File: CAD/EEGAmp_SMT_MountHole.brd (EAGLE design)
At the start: 23.2 x 11.3 mm, 16 parts, among them U1 TL084QD

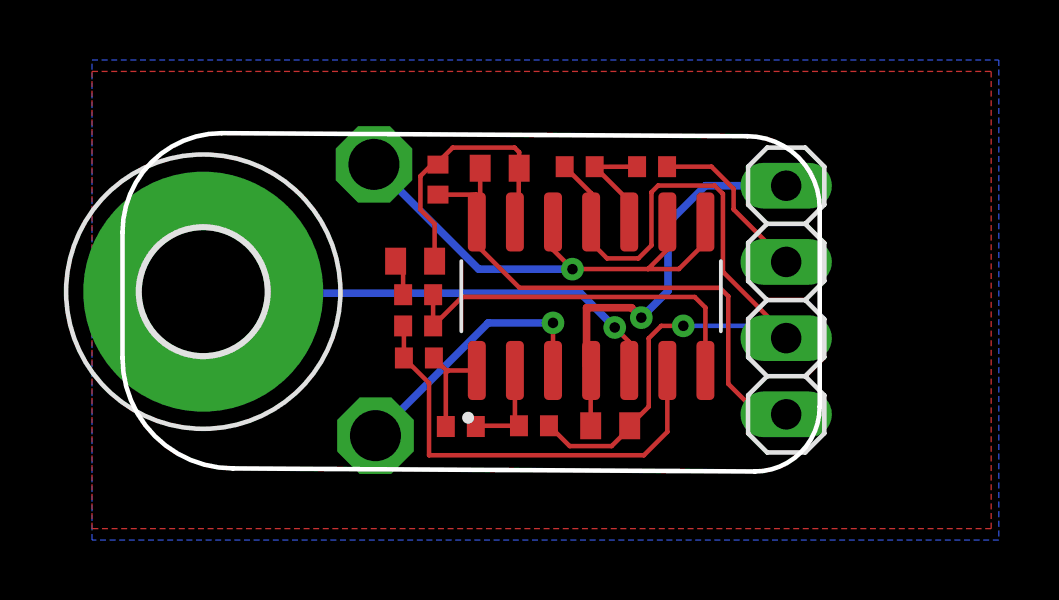
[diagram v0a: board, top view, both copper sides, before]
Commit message: added a filter cap on inputs
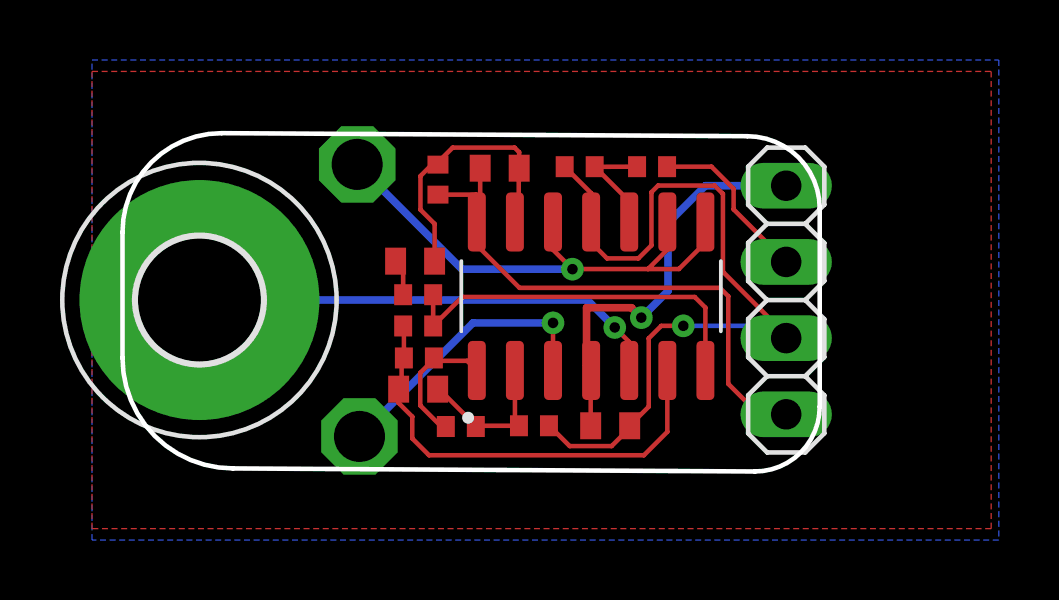
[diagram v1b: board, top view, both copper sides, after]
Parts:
- added C4: 2.2nF, rcl:C0402
- moved REFOUT 0.56 mm to (18.9, 29.8)
- moved AIN- 0.53 mm to (18.9, 20.7)
- moved H1 0.31 mm to (13.6, 25.3)
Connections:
- net 1IN-: now also C4.2
- net 2IN-: now also C4.1
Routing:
- net 1IN-: track 3.36 -> 5.14 mm
- net 1OUT: track 3.49 -> 4.52 mm
- net REFOUT: track 17.2 -> 17.8 mm
- net AIN-: track 9.06 -> 9.61 mm
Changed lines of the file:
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@@
 <plain>
 <text x="19.4564" y="24.638" size="1.778" layer="26" rot="MR0">+</text>
-<text x="16.8832" y="19.993715625" size="1.778" layer="26" rot="MR90">--</text>
+<text x="16.4514" y="19.993715625" size="1.778" layer="26" rot="MR90">--</text>
 <text x="30.018703125" y="29.145721875" size="1.016" layer="26" rot="MR90">V</text>
 <text x="29.983928125" y="24.661759375" size="1.016" layer="26" rot="MR90">VREF</text>
@@
 <attribute name="VALUE" x="29.9974" y="30.353" size="1.27" layer="27" rot="R270"/>
 </element>
-<element name="AIN-" library="testpad" library_urn="urn:adsk.eagle:library:385" package="P1-17" package3d_urn="urn:adsk.eagle:package:27949/1" value="PTR1PAD1-17" x="19.4818" y="20.7518" smashed="yes" rot="R90">
-<attribute name="POPULARITY" value="0" x="19.4818" y="20.7518" size="1.778" layer="27" rot="R90" display="off"/>
-<attribute name="TP_SIGNAL_NAME" value="" x="19.4818" y="20.7518" size="1.778" layer="27" rot="R90" display="off"/>
-</element>
-<element name="H1" library="holes" package="4,1-PAD" value="MOUNT-PAD-ROUND4.1" x="13.7414" y="25.5524" smashed="yes"/>
-<element name="REFOUT" library="testpad" library_urn="urn:adsk.eagle:library:385" package="P1-17" package3d_urn="urn:adsk.eagle:package:27949/1" value="PTR1PAD1-17" x="19.431" y="29.7942" smashed="yes">
-<attribute name="NAME" x="21.8948" y="27.4574" size="0.8128" layer="26" ratio="10" rot="MR0"/>
-<attribute name="POPULARITY" value="0" x="19.558" y="29.7942" size="1.778" layer="27" display="off"/>
-<attribute name="TP_SIGNAL_NAME" value="" x="18.161" y="26.6192" size="1" layer="37"/>
-<attribute name="VALUE" x="24.257" y="37.4142" size="0.0254" layer="27"/>
+<element name="AIN-" library="testpad" library_urn="urn:adsk.eagle:library:385" package="P1-17" package3d_urn="urn:adsk.eagle:package:27949/1" value="PTR1PAD1-17" x="18.9484" y="20.7264" smashed="yes" rot="R90">
+<attribute name="POPULARITY" value="0" x="18.9484" y="20.7264" size="1.778" layer="27" rot="R90" display="off"/>
+<attribute name="TP_SIGNAL_NAME" value="" x="18.9484" y="20.7264" size="1.778" layer="27" rot="R90" display="off"/>
+</element>
+<element name="H1" library="holes" package="4,1-PAD" value="MOUNT-PAD-ROUND4.1" x="13.6144" y="25.273" smashed="yes"/>
+<element name="REFOUT" library="testpad" library_urn="urn:adsk.eagle:library:385" package="P1-17" package3d_urn="urn:adsk.eagle:package:27949/1" value="PTR1PAD1-17" x="18.8722" y="29.7942" smashed="yes">
+<attribute name="NAME" x="21.336" y="27.4574" size="0.8128" layer="26" ratio="10" rot="MR0"/>
+<attribute name="POPULARITY" value="0" x="18.9992" y="29.7942" size="1.778" layer="27" display="off"/>
+<attribute name="TP_SIGNAL_NAME" value="" x="17.6022" y="26.6192" size="1" layer="37"/>
+<attribute name="VALUE" x="23.6982" y="37.4142" size="0.0254" layer="27"/>
+</element>
+<element name="C4" library="rcl" library_urn="urn:adsk.eagle:library:334" package="C0402" package3d_urn="urn:adsk.eagle:package:23626/2" value="2.2nF" x="20.9042" y="22.3012" smashed="yes">
+<attribute name="NAME" x="22.3012" y="21.6916" size="1.27" layer="26" rot="MR0"/>
+<attribute name="POPULARITY" value="16" x="20.9042" y="22.3012" size="1.778" layer="27" display="off"/>
+<attribute name="SPICEPREFIX" value="C" x="20.9042" y="22.3012" size="1.778" layer="27" display="off"/>
 </element>
 </elements>
@@
 <wire x1="25.4" y1="24.511" x2="25.4" y2="22.925" width="0.1524" layer="1"/>
 <contactref element="AIN-" pad="TP"/>
-<wire x1="19.4818" y1="20.7518" x2="23.241" y2="24.511" width="0.254" layer="16"/>
-<wire x1="23.241" y1="24.511" x2="25.4" y2="24.511" width="0.254" layer="16"/>
+<wire x1="18.9484" y1="20.7264" x2="22.733" y2="24.511" width="0.254" layer="16"/>
+<wire x1="22.733" y1="24.511" x2="25.4" y2="24.511" width="0.254" layer="16"/>
 </signal>
 <signal name="VREF">
@@
 <wire x1="27.4574" y1="24.3586" x2="27.94" y2="23.876" width="0.1524" layer="1"/>
 <wire x1="27.94" y1="23.876" x2="27.94" y2="22.925" width="0.1524" layer="1"/>
-<wire x1="27.4574" y1="24.3586" x2="26.3144" y2="25.5016" width="0.254" layer="16"/>
+<wire x1="27.4574" y1="24.3586" x2="26.543" y2="25.273" width="0.254" layer="16"/>
 <contactref element="H1" pad="B4,1"/>
-<wire x1="13.7922" y1="25.5016" x2="13.7414" y2="25.5524" width="0.254" layer="16"/>
-<wire x1="26.3144" y1="25.5016" x2="13.7922" y2="25.5016" width="0.254" layer="16"/>
+<wire x1="26.543" y1="25.273" x2="13.6144" y2="25.273" width="0.254" layer="16"/>
 </signal>
 <signal name="2IN-">
@@
 <wire x1="29.21" y1="22.925" x2="29.21" y2="20.8788" width="0.1524" layer="1"/>
 <wire x1="28.4298" y1="20.0986" x2="21.2678" y2="20.0986" width="0.1524" layer="1"/>
-<wire x1="21.2678" y1="22.5044" x2="20.4296" y2="23.3426" width="0.1524" layer="1"/>
-<wire x1="21.2678" y1="22.5044" x2="21.2678" y2="20.0986" width="0.1524" layer="1"/>
+<wire x1="21.2678" y1="20.0986" x2="20.709" y2="20.6574" width="0.1524" layer="1"/>
+<wire x1="20.709" y1="21.3868" x2="20.709" y2="20.6574" width="0.1524" layer="1"/>
 <wire x1="29.21" y1="20.8788" x2="28.4298" y2="20.0986" width="0.1524" layer="1"/>
 <wire x1="20.4042" y1="24.4094" x2="20.4296" y2="24.384" width="0.1524" layer="1"/>
 <wire x1="20.4296" y1="24.384" x2="20.4296" y2="23.3426" width="0.1524" layer="1"/>
+<contactref element="C4" pad="1"/>
+<wire x1="20.4296" y1="23.3426" x2="20.3534" y2="23.2664" width="0.1524" layer="1"/>
+<wire x1="20.3534" y1="23.2664" x2="20.3534" y2="22.4004" width="0.1524" layer="1"/>
+<wire x1="20.3534" y1="22.4004" x2="20.2542" y2="22.3012" width="0.1524" layer="1"/>
+<wire x1="20.709" y1="21.3868" x2="20.2542" y2="21.8416" width="0.1524" layer="1"/>
+<wire x1="20.2542" y1="22.3012" x2="20.2542" y2="21.8416" width="0.1524" layer="1"/>
 </signal>
 <signal name="3IN+">
@@
 <contactref element="R1" pad="1"/>
 <contactref element="R3" pad="2"/>
-<wire x1="21.898" y1="22.925" x2="22.86" y2="22.925" width="0.1524" layer="1"/>
-<wire x1="21.8266" y1="21.0566" x2="21.8266" y2="22.8536" width="0.1524" layer="1"/>
-<wire x1="21.8266" y1="22.8536" x2="21.8639" y2="22.8909" width="0.1524" layer="1"/>
-<wire x1="21.8639" y1="22.8909" x2="21.898" y2="22.925" width="0.1524" layer="1"/>
-<wire x1="21.4296" y1="23.3426" x2="21.8639" y2="22.9083" width="0.1524" layer="1"/>
-<wire x1="21.8639" y1="22.9083" x2="21.8639" y2="22.8909" width="0.1524" layer="1"/>
+<wire x1="22.86" y1="22.925" x2="22.5385" y2="23.2465" width="0.1524" layer="1"/>
+<wire x1="22.5385" y1="23.2465" x2="21.5257" y2="23.2465" width="0.1524" layer="1"/>
+<wire x1="21.4296" y1="23.3426" x2="21.5257" y2="23.2465" width="0.1524" layer="1"/>
+<wire x1="20.9756" y1="22.8458875" x2="20.9756" y2="21.7565125" width="0.1524" layer="1"/>
+<wire x1="20.9756" y1="21.7565125" x2="21.6683125" y2="21.0638" width="0.1524" layer="1"/>
+<wire x1="21.4296" y1="23.3426" x2="21.4296" y2="23.2998875" width="0.1524" layer="1"/>
+<wire x1="21.6683125" y1="21.0638" x2="21.8194" y2="21.0638" width="0.1524" layer="1"/>
+<wire x1="21.4296" y1="23.2998875" x2="20.9756" y2="22.8458875" width="0.1524" layer="1"/>
+<wire x1="21.8194" y1="21.0638" x2="21.8266" y2="21.0566" width="0.1524" layer="1"/>
 </signal>
 <signal name="VDD">
@@
 <wire x1="22.8266" y1="21.0566" x2="22.8266" y2="21.082" width="0.1524" layer="1"/>
 <wire x1="22.8266" y1="21.082" x2="24.265" y2="21.082" width="0.1524" layer="1"/>
+<contactref element="C4" pad="2"/>
+<wire x1="21.5542" y1="22.3012" x2="21.6074" y2="22.3012" width="0.1524" layer="1"/>
+<wire x1="21.6074" y1="22.3012" x2="22.8266" y2="21.082" width="0.1524" layer="1"/>
 </signal>
 <signal name="4IN-">
@@
 <wire x1="30.48" y1="27.1892" x2="29.5966" y2="26.3058" width="0.1524" layer="1"/>
 <contactref element="REFOUT" pad="TP"/>
-<wire x1="19.431" y1="29.7942" x2="22.9235" y2="26.3017" width="0.254" layer="16"/>
-<wire x1="22.9235" y1="26.3017" x2="26.0477" y2="26.3017" width="0.254" layer="16"/>
+<wire x1="18.8722" y1="29.7942" x2="22.3647" y2="26.3017" width="0.254" layer="16"/>
+<wire x1="22.3647" y1="26.3017" x2="26.0477" y2="26.3017" width="0.254" layer="16"/>
 <via x="26.0477" y="26.3017" extent="1-16" drill="0.35"/>
 </signal>
